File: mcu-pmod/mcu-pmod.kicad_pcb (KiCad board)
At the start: 4 copper layers, 41 x 31 mm, 51 parts, among them J1 PMOD_DEVICE, J2 XILINX_JTAG, J3 CONN_01X03, J4 CONN_01X03, J5 PMOD_HOST, U1 STM32H735-UFBGA176-25, U2 AT24MAC402

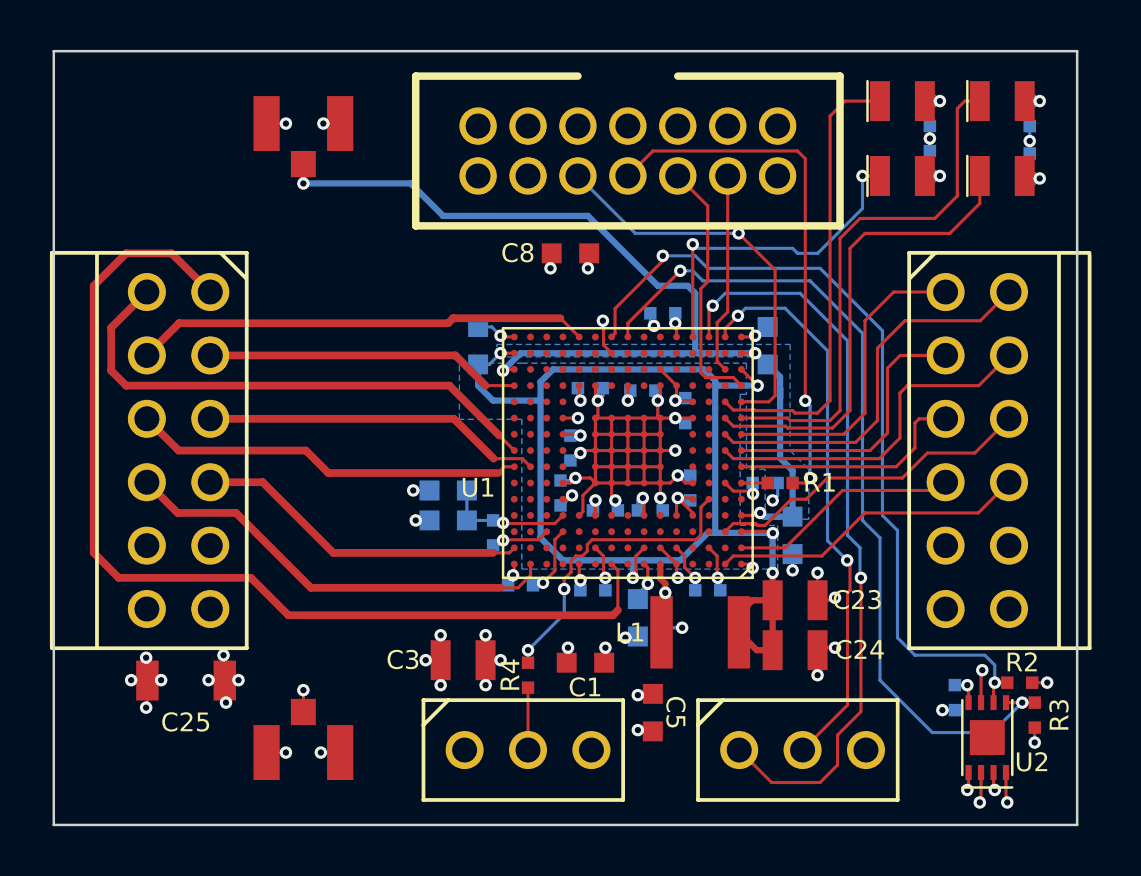
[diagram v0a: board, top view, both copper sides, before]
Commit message: Final rev of mcu-pmod
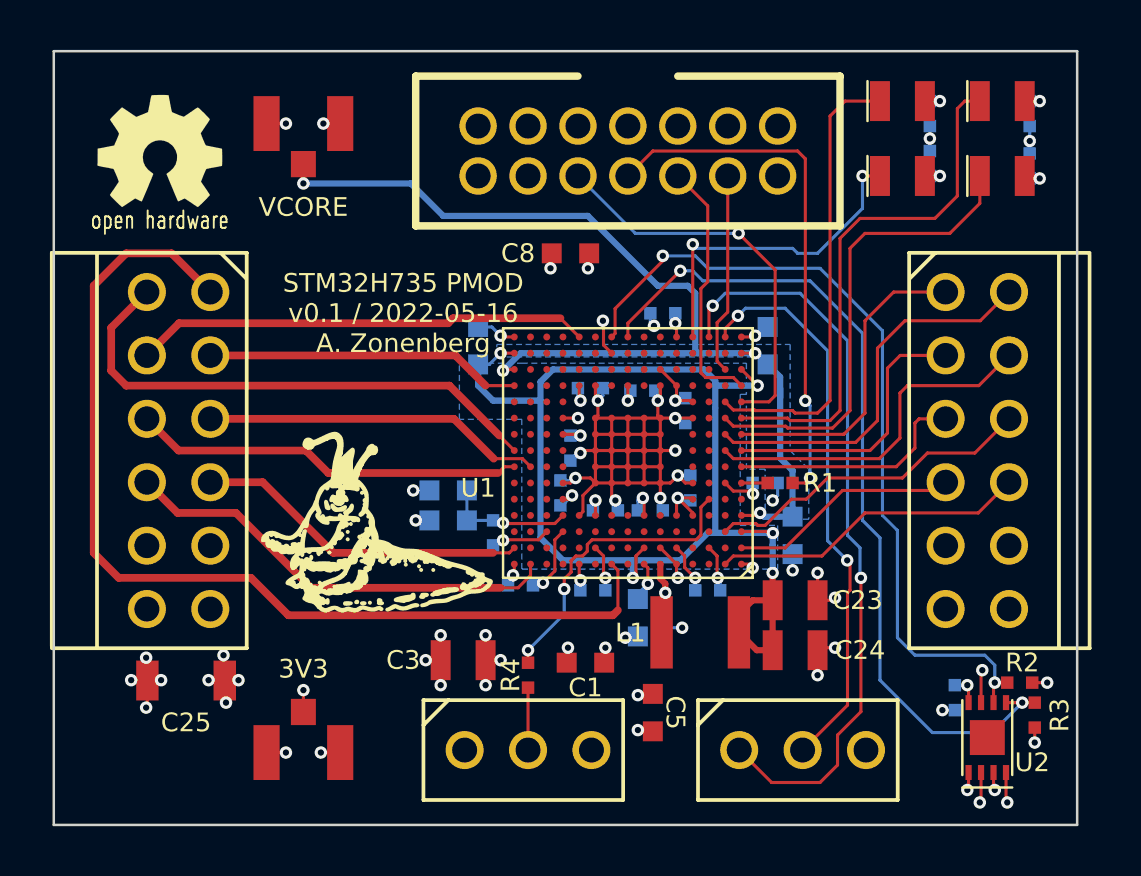
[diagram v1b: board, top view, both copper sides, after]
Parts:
- added G***: LOGO, w_logo:Logo_silk_OSHW_6x6mm, F.Cu at (50.2, 49.0)
- added G***: LOGO, azonenberg_pcb:LONGTHING-1200DPI, F.Cu at (59.5, 64.2)
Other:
- board text added: "3V3"
- board text added: "STM32H735 PMOD v0.1 / 2022-05-16 A. Zonenberg"
- board text added: "VCORE"

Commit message: v0.2 of mcu-pmod with correct STM32 footprint
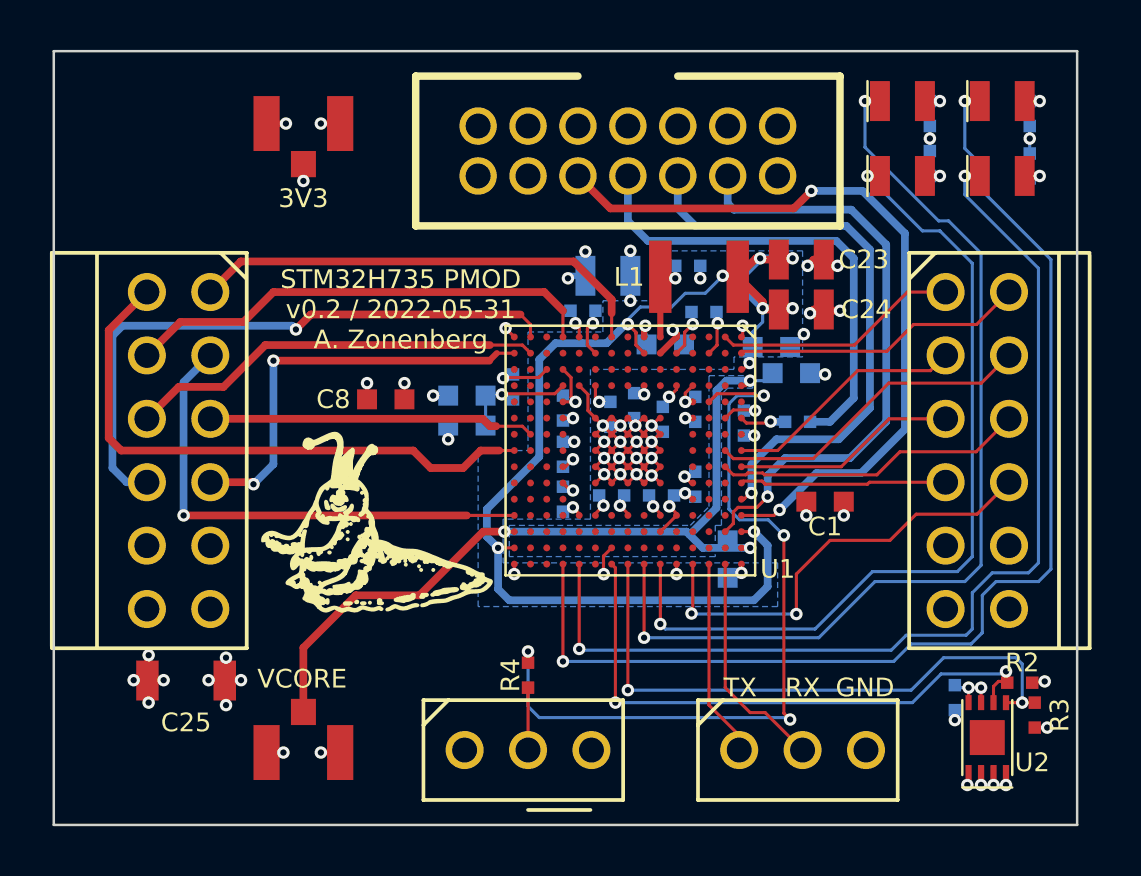
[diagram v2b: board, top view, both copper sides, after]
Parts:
- removed C5: 1 uF, azonenberg_pcb:EIA_0603_CAP_NOSILK
- removed the G*** at (50.2, 49.0)
- C3, R1: moved to B.Cu
- moved C3 16.5 mm to (68.2, 54.0), turned to 180 degrees
- moved L1 14.3 mm to (71.8, 54.0)
- moved C22 14.0 mm to (71.4, 53.6), turned to 0 degrees
- moved C23 13.7 mm to (76.0, 53.4)
- moved C24 13.7 mm to (76.0, 55.4)
- moved C2 11.8 mm to (74.8, 56.9), turned to 0 degrees
- moved C1 11.6 mm to (76.9, 63.0)
- moved C26 11.2 mm to (67.2, 55.4)
- moved C7 11.2 mm to (72.0, 55.5)
- moved C6 11.0 mm to (70.5, 56.8), turned to 0 degrees
- moved C8 9.43 mm to (59.3, 59.0)
- moved C11 8.46 mm to (66.4, 63.0), turned to 90 degrees
- moved C13 5.90 mm to (64.4, 58.5), turned to 90 degrees
- moved C21 5.52 mm to (66.4, 61.1), turned to -90 degrees
- moved C15 4.58 mm to (69.2, 59.2), turned to 90 degrees
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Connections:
- TP1 pad 1: /3V3 -> /VCORE
- TP2 pad 1: /VCORE -> /3V3
- U1 pad A10: /LED0 -> /PMOD_DQ3
- U1 pad A2: /PMOD_DQ3 -> /PMOD_DQ4
- U1 pad A7: /PMOD_DQ2 -> unconnected-(U1-PadA7)
- U1 pad A9: /PMOD_DQ0 -> /PMOD_DQ2
- U1 pad B1: /PMOD_DQ7 -> /PMOD_DQ0
- U1 pad B10: /LED1 -> unconnected-(U1-PadB10)
- U1 pad B11: /LED3 -> unconnected-(U1-PadB11)
- U1 pad B3: /PMOD_DQ6 -> unconnected-(U1-PadB3)
- U1 pad B9: /PMOD_DQ4 -> /PMOD_DQ6
- U1 pad D15: /LED2 -> /PMOD_DQ7
- U1 pad F15: unconnected-(U1-PadF15) -> /LED2
- U1 pad G15: unconnected-(U1-PadG15) -> /LED3
- U1 pad L15: /QSPI_DQ2 -> /LED1
- U1 pad M1: unconnected-(U1-PadM1) -> /QSPI_DQ2
- U1 pad M15: unconnected-(U1-PadM15) -> /LED0
- U1 pad P2: unconnected-(U1-PadP2) -> /QSPI_DQ3
- U1 pad R7: /QSPI_DQ3 -> unconnected-(U1-PadR7)
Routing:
- net /GND: track 260.9 -> 224.9 mm, vias 47 -> 57
- net /LED0: track 21.0 -> 46.6 mm, vias 0 -> 2
- net /LED1: track 19.0 -> 41.4 mm, vias 0 -> 2
- net /UART_TX: track 30.1 -> 7.95 mm, vias 2 -> 0
- net /REFCLK: track 40.6 -> 18.7 mm
- net /LED3: track 18.2 -> 39.0 mm, vias 0 -> 2
- net /LED2: track 13.4 -> 34.1 mm
- net /BOOT0: track 12.2 -> 31.6 mm, vias 2 -> 4
- net /3V3: track 182.9 -> 163.7 mm, vias 31 -> 30
- net /JTAG_TMS: track 8.06 -> 24.3 mm, vias 0 -> 1
- net /JTAG_TDI: track 15.8 -> 30.5 mm, vias 1 -> 2
- net /UART_RX: track 22.6 -> 9.09 mm, vias 2 -> 0
- net /JTAG_TCK: track 10.3 -> 23.3 mm, vias 0 -> 1
- net /I2C_SDA: track 34.3 -> 24.2 mm
- net /I2C_SCL: track 33.1 -> 23.5 mm
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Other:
- board text added: "GND"
- board text added: "RX"
- board text added: "STM32H735 PMOD v0.2 / 2022-05-31 A. Zonenberg"
- board text added: "TX"
- board text removed: "STM32H735 PMOD v0.1 / 2022-05-16 A. Zonenberg"

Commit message: Fixed pin swap
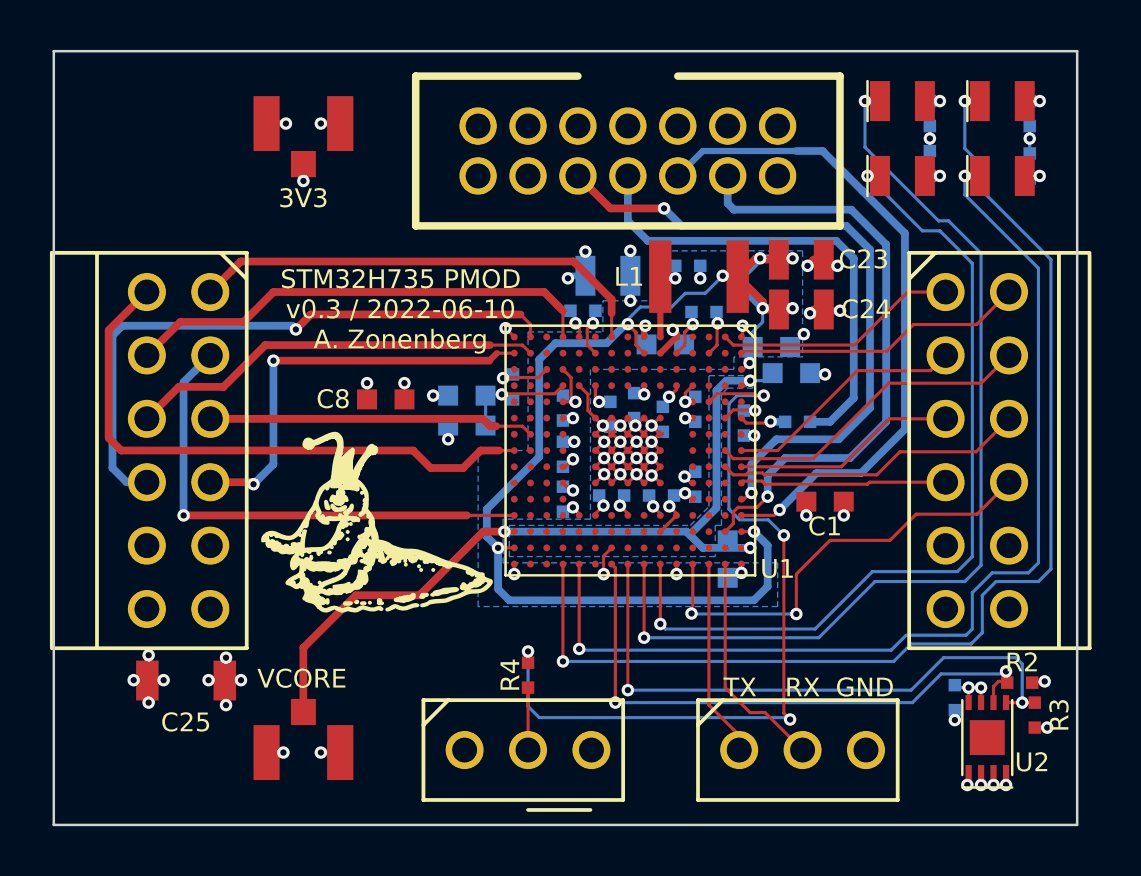
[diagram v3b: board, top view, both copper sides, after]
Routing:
- net /JTAG_TDI: track 30.5 -> 26.6 mm
- net /JTAG_TCK: track 23.3 -> 26.7 mm
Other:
- board text added: "STM32H735 PMOD v0.3 / 2022-06-10 A. Zonenberg"
- board text removed: "STM32H735 PMOD v0.2 / 2022-05-31 A. Zonenberg"
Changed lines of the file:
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@@
       (effects (font (size 1 1) (thickness 0.15)))
     )
-    (fp_line (start -5 -5.1) (end 5 -5.1) (layer "F.SilkS") (width 0.1))
-    (fp_line (start 5 4.9) (end 5 -5.1) (layer "F.SilkS") (width 0.1))
-    (fp_line (start -4.5 -5.1) (end -5 -4.6) (layer "F.SilkS") (width 0.1))
     (fp_line (start -5 4.9) (end 5 4.9) (layer "F.SilkS") (width 0.1))
+    (fp_line (start -4.5 -5.1) (end -5 -4.6) (layer "F.SilkS") (width 0.1))
     (fp_line (start -5 -5.1) (end -5 4.9) (layer "F.SilkS") (width 0.1))
+    (fp_line (start 5 4.9) (end 5 -5.1) (layer "F.SilkS") (width 0.1))
+    (fp_line (start -5 -5.1) (end 5 -5.1) (layer "F.SilkS") (width 0.1))
     (pad "A1" smd circle (at -4.55 -4.55 270) (size 0.275 0.275) (layers "F.Cu" "F.Paste" "F.Mask")
       (net 2 "/GND") (pinfunction "VSS") (pintype "power_in"))
@@
     (pad "A10" smd circle (at 1.3 -4.55 270) (size 0.275 0.275) (layers "F.Cu" "F.Paste" "F.Mask")
       (net 138 "/PMOD_DQ3") (pinfunction "PD1") (pintype "bidirectional"))
-    (pad "A11" smd circle (at 2.6 -4.55 270) (size 0.275 0.275) (layers "F.Cu" "F.Paste" "F.Mask")
+    (pad "A11" smd circle (at 1.95 -4.55 270) (size 0.275 0.275) (layers "F.Cu" "F.Paste" "F.Mask")
       (net 26 "/JTAG_TDI") (pinfunction "JTDI") (pintype "input"))
-    (pad "A12" smd circle (at 1.95 -4.55 270) (size 0.275 0.275) (layers "F.Cu" "F.Paste" "F.Mask")
+    (pad "A12" smd circle (at 2.6 -4.55 270) (size 0.275 0.275) (layers "F.Cu" "F.Paste" "F.Mask")
       (net 24 "/JTAG_TCK") (pinfunction "JTCK") (pintype "input"))
     (pad "A13" smd circle (at 3.25 -4.55 270) (size 0.275 0.275) (layers "F.Cu" "F.Paste" "F.Mask")
@@
     (effects (font (size 0.75 0.75) (thickness 0.1)))
   )
-  (gr_text "STM32H735 PMOD\nv0.2 / 2022-05-31\nA. Zonenberg" (at 59.9 55.35) (layer "F.SilkS")
+  (gr_text "STM32H735 PMOD\nv0.3 / 2022-06-10\nA. Zonenberg" (at 59.9 55.35) (layer "F.SilkS")
     (effects (font (size 0.75 0.75) (thickness 0.1)))
   )
@@
   (segment (start 75.3 61.3) (end 74.6 62) (width 0.31) (layer "B.Cu") (net 23))
   (segment (start 79.35 52.75) (end 79.35 59.85) (width 0.31) (layer "B.Cu") (net 23))
-  (segment (start 73.65 62.95) (end 73.95 62.65) (width 0.125) (layer "F.Cu") (net 24))
-  (segment (start 73.55 62.95) (end 73.65 62.95) (width 0.125) (layer "F.Cu") (net 24))
-  (via (at 73.95 62.7) (size 0.5) (drill 0.25) (layers "F.Cu" "B.Cu") (net 24))
-  (segment (start 71 51.3) (end 71.7 52) (width 0.31) (layer "B.Cu") (net 24))
-  (segment (start 77.75 52) (end 71.7 52) (width 0.31) (layer "B.Cu") (net 24))
-  (segment (start 77.45 60.55) (end 78.7 59.3) (width 0.31) (layer "B.Cu") (net 24))
-  (segment (start 78.7 59.3) (end 78.7 52.95) (width 0.31) (layer "B.Cu") (net 24))
-  (segment (start 74.95 60.55) (end 77.45 60.55) (width 0.31) (layer "B.Cu") (net 24))
-  (segment (start 78.7 52.95) (end 77.75 52) (width 0.31) (layer "B.Cu") (net 24))
-  (segment (start 73.95 62.65) (end 73.95 61.55) (width 0.31) (layer "B.Cu") (net 24))
-  (segment (start 73.95 61.55) (end 74.95 60.55) (width 0.31) (layer "B.Cu") (net 24))
-  (segment (start 71 50) (end 71 51.3) (width 0.31) (layer "B.Cu") (net 24))
+  (segment (start 73.55 63.6) (end 74.857886 63.6) (width 0.125) (layer "F.Cu") (net 24))
+  (segment (start 74.857886 63.6) (end 75.077079 63.380807) (width 0.125) (layer "F.Cu") (net 24))
+  (via (at 75.077079 63.380807) (size 0.5) (drill 0.25) (layers "F.Cu" "B.Cu") (net 24))
+  (segment (start 76.8 49) (end 75.75 49) (width 0.31) (layer "B.Cu") (net 24))
+  (segment (start 80.1 60.15) (end 80.1 52.3) (width 0.31) (layer "B.Cu") (net 24))
+  (segment (start 78.35 61.9) (end 80.1 60.15) (width 0.31) (layer "B.Cu") (net 24))
+  (segment (start 75.077079 63.380807) (end 76.557886 61.9) (width 0.31) (layer "B.Cu") (net 24))
+  (segment (start 78.4 50.6) (end 76.8 49) (width 0.31) (layer "B.Cu") (net 24))
+  (segment (start 80.1 52.3) (end 78.4 50.6) (width 0.31) (layer "B.Cu") (net 24))
+  (segment (start 75.75 49) (end 72 49) (width 0.25) (layer "B.Cu") (net 24))
+  (segment (start 72 49) (end 71 50) (width 0.25) (layer "B.Cu") (net 24))
+  (segment (start 76.557886 61.9) (end 78.35 61.9) (width 0.31) (layer "B.Cu") (net 24))
   (segment (start 69.8 52.6) (end 69 51.8) (width 0.31) (layer "B.Cu") (net 25))
   (segment (start 77.1 59.85) (end 78.05 58.9) (width 0.31) (layer "B.Cu") (net 25))
@@
   (segment (start 69 51.8) (end 69 50) (width 0.31) (layer "B.Cu") (net 25))
   (segment (start 78.05 58.9) (end 78.05 53.3) (width 0.31) (layer "B.Cu") (net 25))
-  (segment (start 73.55 63.6) (end 74.857886 63.6) (width 0.125) (layer "F.Cu") (net 26))
+  (segment (start 73.65 62.95) (end 73.95 62.65) (width 0.125) (layer "F.Cu") (net 26))
   (segment (start 68.3 51.3) (end 67 50) (width 0.31) (layer "F.Cu") (net 26))
-  (segment (start 75.65 51.3) (end 68.3 51.3) (width 0.31) (layer "F.Cu") (net 26))
-  (segment (start 76.35 50.6) (end 75.65 51.3) (width 0.31) (layer "F.Cu") (net 26))
-  (segment (start 74.857886 63.6) (end 75.077079 63.380807) (width 0.125) (layer "F.Cu") (net 26))
-  (via (at 76.35 50.6) (size 0.5) (drill 0.25) (layers "F.Cu" "B.Cu") (net 26))
-  (via (at 75.077079 63.380807) (size 0.5) (drill 0.25) (layers "F.Cu" "B.Cu") (net 26))
-  (segment (start 80.1 60.15) (end 80.1 52.3) (width 0.31) (layer "B.Cu") (net 26))
-  (segment (start 78.35 61.9) (end 80.1 60.15) (width 0.31) (layer "B.Cu") (net 26))
-  (segment (start 75.077079 63.380807) (end 76.557886 61.9) (width 0.31) (layer "B.Cu") (net 26))
-  (segment (start 76.35 50.6) (end 78.4 50.6) (width 0.31) (layer "B.Cu") (net 26))
-  (segment (start 80.1 52.3) (end 78.4 50.6) (width 0.31) (layer "B.Cu") (net 26))
-  (segment (start 76.557886 61.9) (end 78.35 61.9) (width 0.31) (layer "B.Cu") (net 26))
+  (segment (start 70.45 51.3) (end 68.3 51.3) (width 0.31) (layer "F.Cu") (net 26))
+  (segment (start 73.55 62.95) (end 73.65 62.95) (width 0.125) (layer "F.Cu") (net 26))
+  (via (at 73.95 62.7) (size 0.5) (drill 0.25) (layers "F.Cu" "B.Cu") (net 26))
+  (via (at 70.45 51.3) (size 0.5) (drill 0.25) (layers "F.Cu" "B.Cu") (net 26))
+  (segment (start 77.45 60.55) (end 78.7 59.3) (width 0.31) (layer "B.Cu") (net 26))
+  (segment (start 78.7 59.3) (end 78.7 52.95) (width 0.31) (layer "B.Cu") (net 26))
+  (segment (start 77.75 52) (end 71.15 52) (width 0.31) (layer "B.Cu") (net 26))
+  (segment (start 74.95 60.55) (end 77.45 60.55) (width 0.31) (layer "B.Cu") (net 26))
+  (segment (start 78.7 52.95) (end 77.75 52) (width 0.31) (layer "B.Cu") (net 26))
+  (segment (start 73.95 62.65) (end 73.95 61.55) (width 0.31) (layer "B.Cu") (net 26))
+  (segment (start 73.95 61.55) (end 74.95 60.55) (width 0.31) (layer "B.Cu") (net 26))
+  (segment (start 71.15 52) (end 70.45 51.3) (width 0.31) (layer "B.Cu") (net 26))
   (segment (start 72.25 65.55) (end 72.25 71.2) (width 0.125) (layer "F.Cu") (net 30))
   (segment (start 73.46 72.41) (end 73.46 73) (width 0.125) (layer "F.Cu") (net 30))
